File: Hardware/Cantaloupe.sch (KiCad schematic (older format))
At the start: 141 parts, among them J1 OLED, J2 Interconnect, J3 ICSP, J4 OLED, J5 Interconnect_R, J6 ICSP_R, J7 BAT_CON_TOG, J8 BAT_CON_R, J9 BAT_CON, SW1 MX, SW10 MX, SW11 MX, SW12 MX, SW13 MX, SW14 MX, SW15 MX, SW16 MX, SW17 MX, SW18 MX, SW19 MX, SW2 MX, SW20 MX, SW21 MX, SW22 MX, SW23 MX, SW24 MX, SW25 MX, SW26 MX, SW27 MX, SW28 MX, SW29 MX, SW3 MX, SW30 MX, SW31 MX, SW32 Encoder, SW33 Reset, SW34 MX, SW35 MX, SW36 MX, SW37 MX, SW38 MX, SW39 MX, SW4 MX, SW40 MX, SW41 MX, SW42 MX, SW43 MX, SW44 MX, SW45 MX, SW46 MX, SW47 MX, SW48 MX, SW49 MX, SW5 MX, SW50 MX, SW51 MX, SW52 MX, SW53 MX, SW54 MX, SW55 MX, SW56 MX, SW57 MX, SW58 MX, SW59 MX, SW6 MX, SW60 MX, SW61 MX, SW62 MX, SW63 MX, SW64 MX, SW65 Encoder_R, SW66 Reset, SW67 BAT_TOG, SW68 BAT_TOG_R, SW7 MX, SW8 MX, SW9 MX, U1 ProMicro, U2 ProMicro

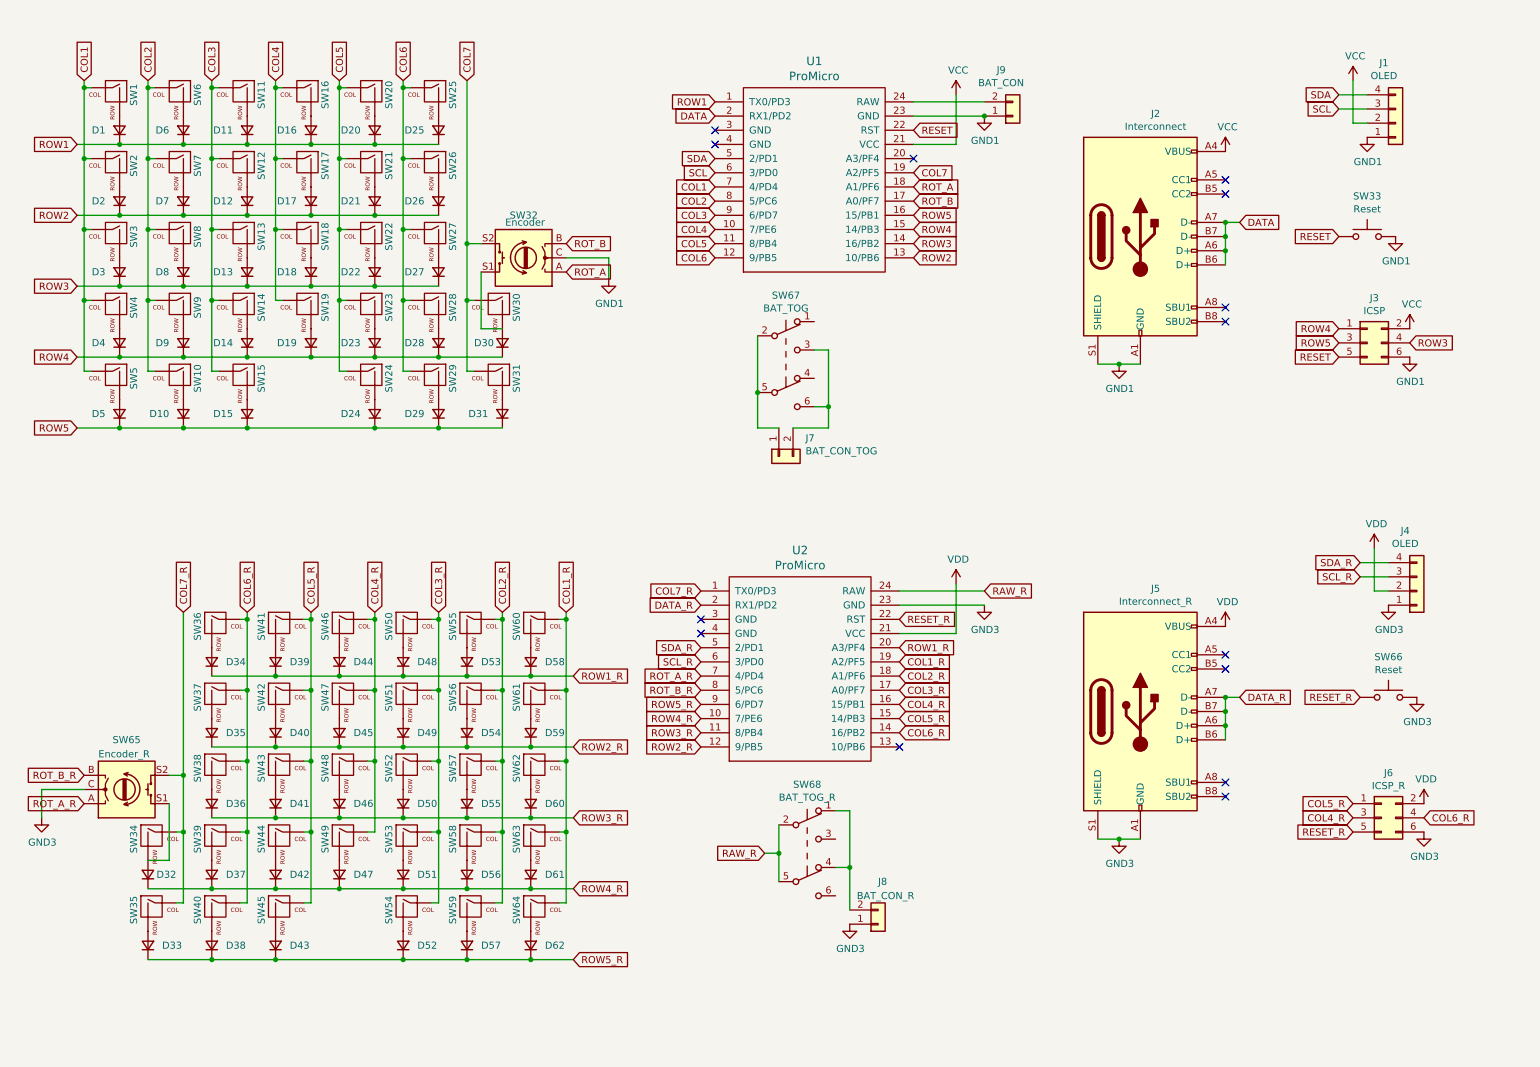
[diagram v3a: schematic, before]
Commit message: Better photo, reorganized footprints, minor fixes to circuit
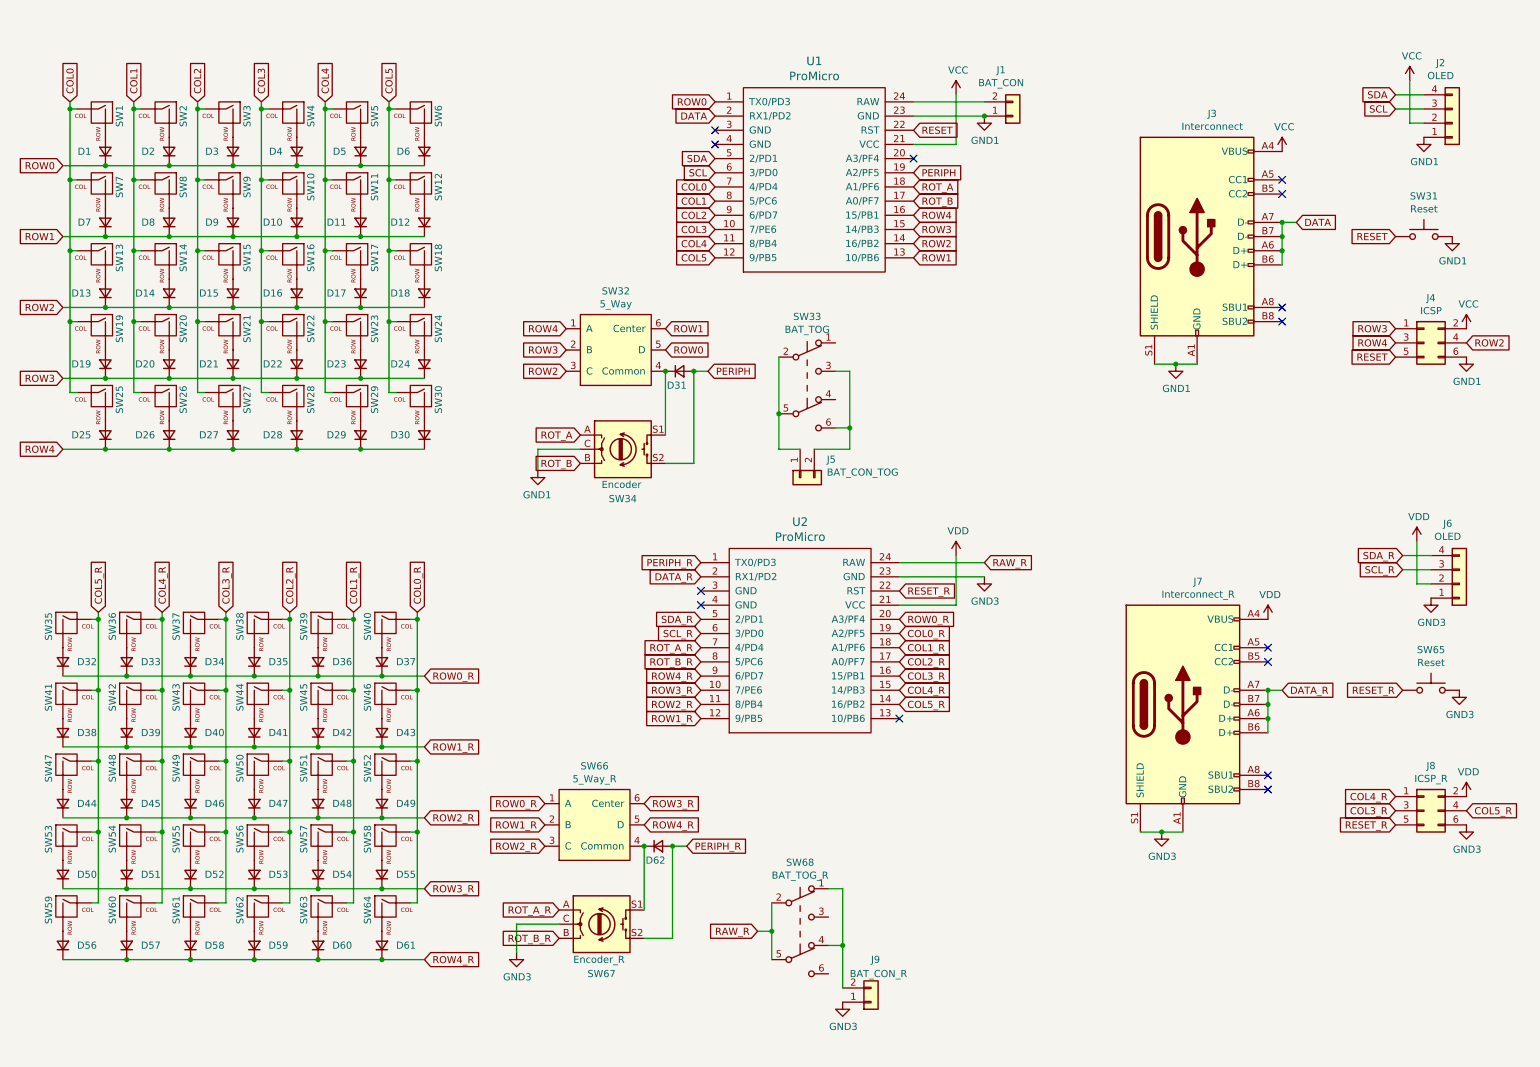
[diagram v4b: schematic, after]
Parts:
- removed D30, D32: D, Diode_SMD:D_SOD-123, symbol Device:D_Small
- removed SW30, SW34: MX, Cantaloupe:CherryMX_Hotswap_SMK, symbol Cantaloupe:MX-NoLED
- added D31, D62: D, Diode_SMD:D_SOD-123, symbol Device:D_Small
- added SW32: 5_Way, Cantaloupe:Switch_5-way-tactile, symbol Cantaloupe:Switch_5-Way-Tactile
- added SW66: 5_Way_R, Cantaloupe:Switch_5-way-tactile, symbol Cantaloupe:Switch_5-Way-Tactile
- SW1, SW23, SW29, SW42, SW64: footprint Cantaloupe:CherryMX_Hotswap_SMK -> Cantaloupe:MX-1U-Hotswap
- SW10: renamed from SW17; footprint Cantaloupe:CherryMX_Hotswap_SMK -> Cantaloupe:MX-1U-Hotswap
- SW11: renamed from SW21; footprint Cantaloupe:CherryMX_Hotswap_SMK -> Cantaloupe:MX-1U-Hotswap
- SW12: renamed from SW26; footprint Cantaloupe:CherryMX_Hotswap_SMK -> Cantaloupe:MX-1U-Hotswap
- SW13: renamed from SW3; footprint Cantaloupe:CherryMX_Hotswap_SMK -> Cantaloupe:MX-1U-Hotswap
- SW14: renamed from SW8; footprint Cantaloupe:CherryMX_Hotswap_SMK -> Cantaloupe:MX-1U-Hotswap
- SW15: renamed from SW13; footprint Cantaloupe:CherryMX_Hotswap_SMK -> Cantaloupe:MX-1U-Hotswap
- SW16: renamed from SW18; footprint Cantaloupe:CherryMX_Hotswap_SMK -> Cantaloupe:MX-1U-Hotswap
- SW17: renamed from SW22; footprint Cantaloupe:CherryMX_Hotswap_SMK -> Cantaloupe:MX-1U-Hotswap
- SW18: renamed from SW27; footprint Cantaloupe:CherryMX_Hotswap_SMK -> Cantaloupe:MX-1U-Hotswap
- SW19: renamed from SW4; footprint Cantaloupe:CherryMX_Hotswap_SMK -> Cantaloupe:MX-1U-Hotswap
- SW2: renamed from SW6; footprint Cantaloupe:CherryMX_Hotswap_SMK -> Cantaloupe:MX-1U-Hotswap
- SW20: renamed from SW9; footprint Cantaloupe:CherryMX_Hotswap_SMK -> Cantaloupe:MX-1U-Hotswap
- SW21: renamed from SW14; footprint Cantaloupe:CherryMX_Hotswap_SMK -> Cantaloupe:MX-1U-Hotswap
- SW22: renamed from SW19; footprint Cantaloupe:CherryMX_Hotswap_SMK -> Cantaloupe:MX-1U-Hotswap
- SW24: renamed from SW28; footprint Cantaloupe:CherryMX_Hotswap_SMK -> Cantaloupe:MX-1U-Hotswap
- SW25: renamed from SW5; footprint Cantaloupe:CherryMX_Hotswap_SMK -> Cantaloupe:MX-1U-Hotswap
- SW26: renamed from SW10; footprint Cantaloupe:CherryMX_Hotswap_SMK -> Cantaloupe:MX-1U-Hotswap
- SW27: renamed from SW15; footprint Cantaloupe:CherryMX_Hotswap_SMK -> Cantaloupe:MX-1U-Hotswap
- SW28: renamed from SW24; footprint Cantaloupe:CherryMX_Hotswap_SMK -> Cantaloupe:MX-1U-Hotswap
- SW3: renamed from SW11; footprint Cantaloupe:CherryMX_Hotswap_SMK -> Cantaloupe:MX-1U-Hotswap
- SW30: renamed from SW31; footprint Cantaloupe:CherryMX_Hotswap_SMK -> Cantaloupe:MX-1U-Hotswap
- SW35: renamed from SW36; footprint Cantaloupe:CherryMX_Hotswap_SMK -> Cantaloupe:MX-1U-Hotswap
- SW36: renamed from SW41; footprint Cantaloupe:CherryMX_Hotswap_SMK -> Cantaloupe:MX-1U-Hotswap
- SW37: renamed from SW46; footprint Cantaloupe:CherryMX_Hotswap_SMK -> Cantaloupe:MX-1U-Hotswap
- SW38: renamed from SW50; footprint Cantaloupe:CherryMX_Hotswap_SMK -> Cantaloupe:MX-1U-Hotswap
- SW39: renamed from SW55; footprint Cantaloupe:CherryMX_Hotswap_SMK -> Cantaloupe:MX-1U-Hotswap
- SW4: renamed from SW16; footprint Cantaloupe:CherryMX_Hotswap_SMK -> Cantaloupe:MX-1U-Hotswap
- SW40: renamed from SW60; footprint Cantaloupe:CherryMX_Hotswap_SMK -> Cantaloupe:MX-1U-Hotswap
- SW41: renamed from SW37; footprint Cantaloupe:CherryMX_Hotswap_SMK -> Cantaloupe:MX-1U-Hotswap
- SW43: renamed from SW47; footprint Cantaloupe:CherryMX_Hotswap_SMK -> Cantaloupe:MX-1U-Hotswap
- SW44: renamed from SW51; footprint Cantaloupe:CherryMX_Hotswap_SMK -> Cantaloupe:MX-1U-Hotswap
- SW45: renamed from SW56; footprint Cantaloupe:CherryMX_Hotswap_SMK -> Cantaloupe:MX-1U-Hotswap
- SW46: renamed from SW61; footprint Cantaloupe:CherryMX_Hotswap_SMK -> Cantaloupe:MX-1U-Hotswap
- SW47: renamed from SW38; footprint Cantaloupe:CherryMX_Hotswap_SMK -> Cantaloupe:MX-1U-Hotswap
- SW48: renamed from SW43; footprint Cantaloupe:CherryMX_Hotswap_SMK -> Cantaloupe:MX-1U-Hotswap
- SW49: renamed from SW48; footprint Cantaloupe:CherryMX_Hotswap_SMK -> Cantaloupe:MX-1U-Hotswap
- SW5: renamed from SW20; footprint Cantaloupe:CherryMX_Hotswap_SMK -> Cantaloupe:MX-1U-Hotswap
- SW50: renamed from SW52; footprint Cantaloupe:CherryMX_Hotswap_SMK -> Cantaloupe:MX-1U-Hotswap
- SW51: renamed from SW57; footprint Cantaloupe:CherryMX_Hotswap_SMK -> Cantaloupe:MX-1U-Hotswap
- SW52: renamed from SW62; footprint Cantaloupe:CherryMX_Hotswap_SMK -> Cantaloupe:MX-1U-Hotswap
- SW53: renamed from SW39; footprint Cantaloupe:CherryMX_Hotswap_SMK -> Cantaloupe:MX-1U-Hotswap
- SW54: renamed from SW44; footprint Cantaloupe:CherryMX_Hotswap_SMK -> Cantaloupe:MX-1U-Hotswap
- SW55: renamed from SW49; footprint Cantaloupe:CherryMX_Hotswap_SMK -> Cantaloupe:MX-1U-Hotswap
- SW56: renamed from SW53; footprint Cantaloupe:CherryMX_Hotswap_SMK -> Cantaloupe:MX-1U-Hotswap
- SW57: renamed from SW58; footprint Cantaloupe:CherryMX_Hotswap_SMK -> Cantaloupe:MX-1U-Hotswap
- SW58: renamed from SW63; footprint Cantaloupe:CherryMX_Hotswap_SMK -> Cantaloupe:MX-1U-Hotswap
- SW59: renamed from SW35; footprint Cantaloupe:CherryMX_Hotswap_SMK -> Cantaloupe:MX-1U-Hotswap
- SW6: renamed from SW25; footprint Cantaloupe:CherryMX_Hotswap_SMK -> Cantaloupe:MX-1U-Hotswap
- SW60: renamed from SW40; footprint Cantaloupe:CherryMX_Hotswap_SMK -> Cantaloupe:MX-1U-Hotswap
- SW61: renamed from SW45; footprint Cantaloupe:CherryMX_Hotswap_SMK -> Cantaloupe:MX-1U-Hotswap
- SW62: renamed from SW54; footprint Cantaloupe:CherryMX_Hotswap_SMK -> Cantaloupe:MX-1U-Hotswap
- SW63: renamed from SW59; footprint Cantaloupe:CherryMX_Hotswap_SMK -> Cantaloupe:MX-1U-Hotswap
- SW7: renamed from SW2; footprint Cantaloupe:CherryMX_Hotswap_SMK -> Cantaloupe:MX-1U-Hotswap
- SW8: renamed from SW7; footprint Cantaloupe:CherryMX_Hotswap_SMK -> Cantaloupe:MX-1U-Hotswap
- SW9: renamed from SW12; footprint Cantaloupe:CherryMX_Hotswap_SMK -> Cantaloupe:MX-1U-Hotswap
- renumbered D17 to D10, D21 to D11, D26 to D12, D3 to D13, D8 to D14, D13 to D15, D18 to D16, D22 to D17, D27 to D18, D4 to D19, D6 to D2, D9 to D20, D14 to D21, D19 to D22, D28 to D24, D5 to D25, D10 to D26, D15 to D27, D24 to D28, D11 to D3, D31 to D30, D34 to D32, D39 to D33, D44 to D34, D48 to D35, D53 to D36, D58 to D37, D35 to D38, D40 to D39, D16 to D4, D45 to D40, D49 to D41, D54 to D42, D59 to D43, D36 to D44, D41 to D45, D50 to D47, D55 to D48, D60 to D49, D20 to D5, D37 to D50, D42 to D51, D47 to D52, D51 to D53, D56 to D54, D61 to D55, D33 to D56, D38 to D57, D43 to D58, D52 to D59, D25 to D6, D57 to D60, D62 to D61, D2 to D7, D7 to D8, D12 to D9, J9 to J1, J1 to J2, J2 to J3, J3 to J4, J7 to J5, J4 to J6, J5 to J7, J6 to J8, J8 to J9, SW33 to SW31, SW67 to SW33, SW32 to SW34, SW66 to SW65, SW65 to SW67
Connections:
- net ROW5 is gone; now on net ROW4: D25.1 (K), D26.1 (K), D27.1 (K), D28.1 (K), D29.1 (K), D30.1 (K), J4.3 (Pin_3), U1.16 (15/PB1)
- net ROW5_R is gone; now on net ROW4_R: D56.1 (K), D57.1 (K), D58.1 (K), D59.1 (K), D60.1 (K), D61.1 (K), U2.9 (6/PD7)
- net COL1: now also SW14.1 (COL), SW2.1 (COL), SW20.1 (COL), SW26.1 (COL), SW8.1 (COL), U1.8 (5/PC6); no longer SW1.1 (COL), SW13.1 (COL), SW19.1 (COL), SW25.1 (COL), SW7.1 (COL), U1.7 (4/PD4)
- net COL1_R: now also SW39.1 (COL), SW45.1 (COL), SW51.1 (COL), SW57.1 (COL), SW63.1 (COL), U2.18 (A1/PF6); no longer SW40.1 (COL), SW46.1 (COL), SW52.1 (COL), SW58.1 (COL), SW64.1 (COL), U2.19 (A2/PF5)
- net COL2: now also SW15.1 (COL), SW21.1 (COL), SW27.1 (COL), SW3.1 (COL), SW9.1 (COL), U1.9 (6/PD7); no longer SW14.1 (COL), SW2.1 (COL), SW20.1 (COL), SW26.1 (COL), SW8.1 (COL), U1.8 (5/PC6)
- net COL2_R: now also SW38.1 (COL), SW44.1 (COL), SW50.1 (COL), SW56.1 (COL), SW62.1 (COL), U2.17 (A0/PF7); no longer SW39.1 (COL), SW45.1 (COL), SW51.1 (COL), SW57.1 (COL), SW63.1 (COL), U2.18 (A1/PF6)
- net COL3: now also SW10.1 (COL), SW16.1 (COL), SW22.1 (COL), SW28.1 (COL), SW4.1 (COL), U1.10 (7/PE6); no longer SW15.1 (COL), SW21.1 (COL), SW27.1 (COL), SW3.1 (COL), SW9.1 (COL), U1.9 (6/PD7)
- net COL3_R: now also J8.3 (Pin_3), SW37.1 (COL), SW43.1 (COL), SW49.1 (COL), SW55.1 (COL), SW61.1 (COL), U2.16 (15/PB1); no longer SW38.1 (COL), SW44.1 (COL), SW50.1 (COL), SW56.1 (COL), SW62.1 (COL), U2.17 (A0/PF7)
- net COL4: now also SW11.1 (COL), SW17.1 (COL), SW23.1 (COL), SW29.1 (COL), SW5.1 (COL), U1.11 (8/PB4); no longer SW10.1 (COL), SW16.1 (COL), SW22.1 (COL), SW4.1 (COL), U1.10 (7/PE6)
- net COL4_R: now also J8.1 (Pin_1), SW36.1 (COL), SW42.1 (COL), SW48.1 (COL), SW54.1 (COL), SW60.1 (COL), U2.15 (14/PB3); no longer J8.3 (Pin_3), SW37.1 (COL), SW43.1 (COL), SW49.1 (COL), SW55.1 (COL), U2.16 (15/PB1)
- net COL5: now also SW12.1 (COL), SW18.1 (COL), SW24.1 (COL), SW30.1 (COL), SW6.1 (COL), U1.12 (9/PB5); no longer SW11.1 (COL), SW17.1 (COL), SW23.1 (COL), SW28.1 (COL), SW5.1 (COL), U1.11 (8/PB4)
- net COL5_R: now also J8.4 (Pin_4), SW35.1 (COL), SW41.1 (COL), SW47.1 (COL), SW53.1 (COL), SW59.1 (COL), U2.14 (16/PB2); no longer J8.1 (Pin_1), SW36.1 (COL), SW42.1 (COL), SW48.1 (COL), SW54.1 (COL), SW61.1 (COL), U2.15 (14/PB3)
- net ROW1: now also D10.1 (K), D11.1 (K), D12.1 (K), D7.1 (K), D8.1 (K), D9.1 (K), U1.13 (10/PB6), SW32.6 (Center); no longer D1.1 (K), D2.1 (K), D3.1 (K), D4.1 (K), D5.1 (K), D6.1 (K), U1.1 (TX0/PD3)
- net ROW1_R: now also D38.1 (K), D39.1 (K), D40.1 (K), D41.1 (K), D42.1 (K), D43.1 (K), U2.12 (9/PB5), SW66.2 (B); no longer D32.1 (K), D33.1 (K), D34.1 (K), D35.1 (K), D36.1 (K), D37.1 (K), U2.20 (A3/PF4)
- net ROW2: now also D13.1 (K), D14.1 (K), D15.1 (K), D16.1 (K), D17.1 (K), D18.1 (K), J4.4 (Pin_4), U1.14 (16/PB2), SW32.3 (C); no longer D10.1 (K), D11.1 (K), D12.1 (K), D7.1 (K), D8.1 (K), D9.1 (K), U1.13 (10/PB6)
- net ROW2_R: now also D44.1 (K), D45.1 (K), D46.1 (K), D47.1 (K), D48.1 (K), D49.1 (K), U2.11 (8/PB4), SW66.3 (C); no longer D38.1 (K), D39.1 (K), D40.1 (K), D41.1 (K), D42.1 (K), D43.1 (K), U2.12 (9/PB5)
- net ROW3: now also D19.1 (K), D20.1 (K), D21.1 (K), D22.1 (K), D23.1 (K), D24.1 (K), J4.1 (Pin_1), U1.15 (14/PB3), SW32.2 (B); no longer D13.1 (K), D14.1 (K), D15.1 (K), D16.1 (K), D17.1 (K), D18.1 (K), J4.4 (Pin_4), U1.14 (16/PB2)
- net ROW3_R: now also D50.1 (K), D51.1 (K), D52.1 (K), D53.1 (K), D54.1 (K), D55.1 (K), U2.10 (7/PE6), SW66.6 (Center); no longer D44.1 (K), D45.1 (K), D46.1 (K), D47.1 (K), D48.1 (K), D49.1 (K), U2.11 (8/PB4)
- net ROW4: now also SW32.1 (A); no longer D19.1 (K), D20.1 (K), D21.1 (K), D22.1 (K), D23.1 (K), D24.1 (K), J4.1 (Pin_1), U1.15 (14/PB3)
- net ROW4_R: now also SW66.5 (D); no longer D50.1 (K), D51.1 (K), D52.1 (K), D53.1 (K), D54.1 (K), D55.1 (K), U2.10 (7/PE6)
- net at SW34.S1: now also D31.1 (K), SW32.4 (Common)
- net at SW67.S1: now also D62.1 (K), SW66.4 (Common)
- removed net COL6: SW12.1 (COL), SW18.1 (COL), SW24.1 (COL), SW29.1 (COL), SW6.1 (COL), U1.12 (9/PB5)
- removed net COL6_R: J8.4 (Pin_4), SW35.1 (COL), SW41.1 (COL), SW47.1 (COL), SW53.1 (COL), SW60.1 (COL), U2.14 (16/PB2)
- net COL7 renamed PERIPH
- net PERIPH: now also D31.2 (A); no longer SW30.1 (COL)
- net COL7_R renamed PERIPH_R
- net PERIPH_R: now also D62.2 (A); no longer SW59.1 (COL)
- new net COL0: SW1.1 (COL), SW13.1 (COL), SW19.1 (COL), SW25.1 (COL), SW7.1 (COL), U1.7 (4/PD4)
- new net COL0_R: SW40.1 (COL), SW46.1 (COL), SW52.1 (COL), SW58.1 (COL), SW64.1 (COL), U2.19 (A2/PF5)
- new net ROW0: D1.1 (K), D2.1 (K), D3.1 (K), D4.1 (K), D5.1 (K), D6.1 (K), SW32.5 (D), U1.1 (TX0/PD3)
- new net ROW0_R: D32.1 (K), D33.1 (K), D34.1 (K), D35.1 (K), D36.1 (K), D37.1 (K), SW66.1 (A), U2.20 (A3/PF4)
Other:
- moved on the sheet: D1, D10, D11, D12, D13, D14, D15, D16, D17, D18, D19, D2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

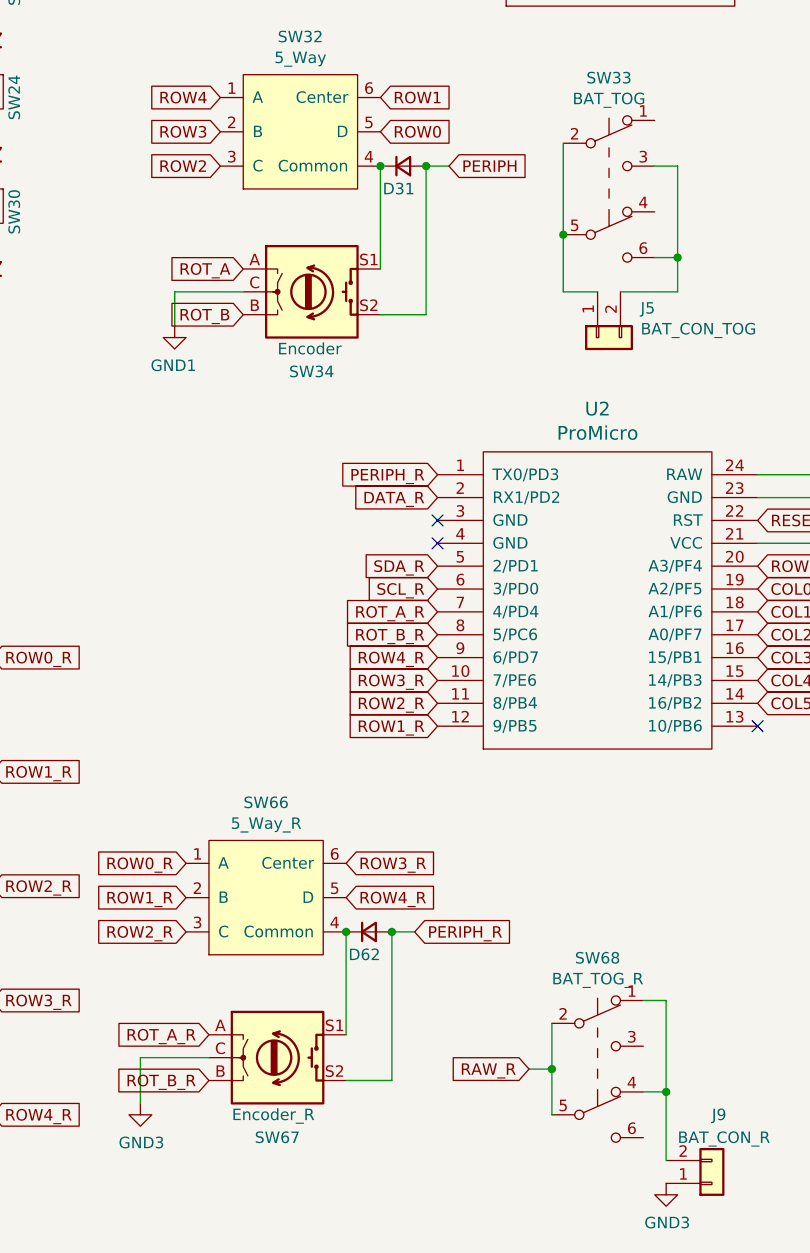
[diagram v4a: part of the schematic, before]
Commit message: Fixed position of RHS screw hole and wiring of rotary encoder switch, added QMK firmware.
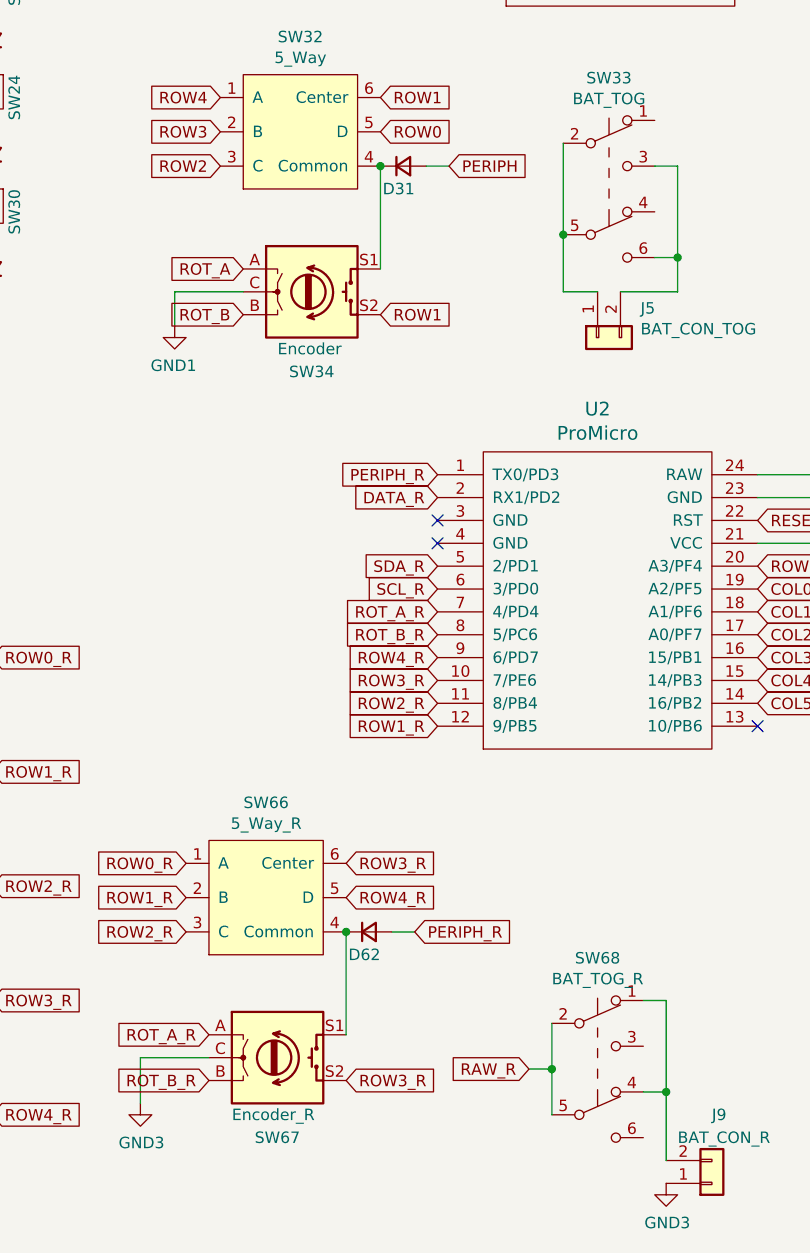
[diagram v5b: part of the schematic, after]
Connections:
- net PERIPH: no longer SW34.S2
- net PERIPH_R: no longer SW67.S2
- net ROW1: now also SW34.S2
- net ROW3_R: now also SW67.S2
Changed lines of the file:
@@
 Text GLabel 5300 5000 0    50   Input ~ 0
 ROT_B_R
-Text GLabel 4300 6750 0    50   Input ~ 0
-ROT_A_R
 Wire Wire Line
 	4300 6850 4000 6850
-$Comp
-L Device:Rotary_Encoder_Switch SW67
-U 1 1 5FC9B861
-P 4600 6850
-F 0 "SW67" H 4500 6500 50  0000 L CNN
-F 1 "Encoder_R" H 4400 6600 50  0000 L CNN
-F 2 "Rotary_Encoder:RotaryEncoder_Alps_EC11E-Switch_Vertical_H20mm" H 4450 7010 50  0001 C CNN
-F 3 "~" H 4600 7110 50  0001 C CNN
-	1    4600 6850
-	1    0    0    -1
-$EndComp
-Text GLabel 4300 6950 0    50   Input ~ 0
-ROT_B_R
 Text GLabel 3300 4650 1    50   Input ~ 0
 COL0_R
@@
 Wire Wire Line
 	3150 3100 3100 3100
-Text GLabel 4450 3400 0    50   Input ~ 0
-ROT_A
 Wire Wire Line
 	4450 3500 4150 3500
-$Comp
-L Device:Rotary_Encoder_Switch SW34
-U 1 1 5F7FDE64
-P 4750 3500
-F 0 "SW34" H 4650 3150 50  0000 L CNN
-F 1 "Encoder" H 4600 3250 50  0000 L CNN
-F 2 "Rotary_Encoder:RotaryEncoder_Alps_EC11E-Switch_Vertical_H20mm" H 4600 3660 50  0001 C CNN
-F 3 "~" H 4750 3760 50  0001 C CNN
-	1    4750 3500
-	1    0    0    -1
-$EndComp
 $Comp
 L Cantaloupe:MX-NoLED SW30
@@
 	0    1    -1   0
 $EndComp
-Text GLabel 4450 3600 0    50   Input ~ 0
-ROT_B
 Text GLabel 3350 5600 2    50   Input ~ 0
 ROW1_R
@@
 Text GLabel 5400 1650 0    50   Input ~ 0
 COL0
-$Comp
-L Device:D_Small D31
-U 1 1 5FC9F973
-P 5150 2950
-F 0 "D31" H 5200 2850 50  0000 R CNN
-F 1 "D" V 5105 2871 50  0001 R CNN
-F 2 "Diode_SMD:D_SOD-123" H 5150 2950 50  0001 C CNN
-F 3 "~" H 5150 2950 50  0001 C CNN
-	1    5150 2950
-	1    0    0    -1
-$EndComp
-Text GLabel 5350 2950 2    50   Input ~ 0
-PERIPH
 Text GLabel 6800 1550 2    50   Input ~ 0
 PERIPH
-Text GLabel 5050 2800 2    50   Input ~ 0
-ROW0
-Text GLabel 5050 2650 2    50   Input ~ 0
-ROW1
-Text GLabel 4350 2800 0    50   Input ~ 0
-ROW3
-Text GLabel 4350 2950 0    50   Input ~ 0
-ROW2
-Text GLabel 4350 2650 0    50   Input ~ 0
-ROW4
-Wire Wire Line
-	5250 3600 5050 3600
-Wire Wire Line
-	5350 2950 5250 2950
-Connection ~ 5250 2950
 $Comp
 L Device:D_Small D62
@@
 Text GLabel 5300 4300 0    50   Input ~ 0
 PERIPH_R
-Wire Wire Line
-	4900 6300 4900 6750
-Wire Wire Line
-	5100 6300 5100 6950
-Wire Wire Line
-	5100 6950 4900 6950
-Connection ~ 5100 6300
 $Comp
 L Cantaloupe:Switch_5-Way-Tactile SW66
@@
 	1    0    0    -1
 $EndComp
-Connection ~ 4900 6300
-Wire Wire Line
-	5050 2950 5050 3400
-Wire Wire Line
-	5250 2950 5250 3600
-$Comp
-L Cantaloupe:Switch_5-Way-Tactile SW32
-U 1 1 5FEC203F
-P 4700 2800
-F 0 "SW32" H 4700 3215 50  0000 C CNN
-F 1 "5_Way" H 4700 3124 50  0000 C CNN
-F 2 "Cantaloupe:Switch_5-way-tactile" H 4700 3250 50  0001 C CNN
-F 3 "" H 4700 3250 50  0001 C CNN
-	1    4700 2800
-	1    0    0    -1
-$EndComp
-Connection ~ 5050 2950
 Text GLabel 10700 2750 2    50   Input ~ 0
 ROW2
@@
 Text GLabel 4900 6000 2    50   Input ~ 0
 ROW3_R
+$Comp
+L Cantaloupe:Switch_5-Way-Tactile SW32
+U 1 1 5FEC203F
+P 4700 2800
+F 0 "SW32" H 4700 3215 50  0000 C CNN
+F 1 "5_Way" H 4700 3124 50  0000 C CNN
+F 2 "Cantaloupe:Switch_5-way-tactile" H 4700 3250 50  0001 C CNN
+F 3 "" H 4700 3250 50  0001 C CNN
+	1    4700 2800
+	1    0    0    -1
+$EndComp
+Wire Wire Line
+	5350 2950 5250 2950
+Text GLabel 4350 2650 0    50   Input ~ 0
+ROW4
+Text GLabel 4350 2950 0    50   Input ~ 0
+ROW2
+Text GLabel 4350 2800 0    50   Input ~ 0
+ROW3
+Text GLabel 5050 2650 2    50   Input ~ 0
+ROW1
+Text GLabel 5050 2800 2    50   Input ~ 0
+ROW0
+Text GLabel 5350 2950 2    50   Input ~ 0
+PERIPH
+$Comp
+L Device:D_Small D31
+U 1 1 5FC9F973
+P 5150 2950
+F 0 "D31" H 5200 2850 50  0000 R CNN
+F 1 "D" V 5105 2871 50  0001 R CNN
+F 2 "Diode_SMD:D_SOD-123" H 5150 2950 50  0001 C CNN
+F 3 "~" H 5150 2950 50  0001 C CNN
+	1    5150 2950
+	1    0    0    -1
+$EndComp
+Text GLabel 4300 6950 0    50   Input ~ 0
+ROT_B_R
+Text GLabel 4300 6750 0    50   Input ~ 0
+ROT_A_R
+$Comp
+L Device:Rotary_Encoder_Switch SW67
+U 1 1 5FC9B861
+P 4600 6850
+F 0 "SW67" H 4500 6500 50  0000 L CNN
+F 1 "Encoder_R" H 4400 6600 50  0000 L CNN
+F 2 "Rotary_Encoder:RotaryEncoder_Alps_EC11E-Switch_Vertical_H20mm" H 4450 7010 50  0001 C CNN
+F 3 "~" H 4600 7110 50  0001 C CNN
+	1    4600 6850
+	1    0    0    -1
+$EndComp
+Text GLabel 4450 3600 0    50   Input ~ 0
+ROT_B
+Text GLabel 4450 3400 0    50   Input ~ 0
+ROT_A
+$Comp
+L Device:Rotary_Encoder_Switch SW34
+U 1 1 5F7FDE64
+P 4750 3500
+F 0 "SW34" H 4650 3150 50  0000 L CNN
+F 1 "Encoder" H 4600 3250 50  0000 L CNN
+F 2 "Rotary_Encoder:RotaryEncoder_Alps_EC11E-Switch_Vertical_H20mm" H 4600 3660 50  0001 C CNN
+F 3 "~" H 4750 3760 50  0001 C CNN
+	1    4750 3500
+	1    0    0    -1
+$EndComp
+Wire Wire Line
+	5050 3400 5050 2950
+Connection ~ 5050 2950
+Text GLabel 5050 3600 2    50   Input ~ 0
+ROW1
+Wire Wire Line
+	4900 6750 4900 6300
+Connection ~ 4900 6300
+Text GLabel 4900 6950 2    50   Input ~ 0
+ROW3_R
 $EndSCHEMATC
